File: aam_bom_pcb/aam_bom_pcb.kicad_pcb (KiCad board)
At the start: 4 copper layers, 58 x 19.5 mm, 42 parts, among them J1 USB_C_Receptacle_USB2.0_16P, U1 BQ25120AYFPR, U3 STM32WB5MMG, U4 TLV320DAC3203IRGER

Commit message: Actualización: integración de nuevos archivos al proyecto principal
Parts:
- moved TP6 23.1 mm to (179.9, 54.0)
- moved TP7 21.3 mm to (180.4, 50.5)
- moved C9 19.6 mm to (194.5, 52.5), turned to 180 degrees
- moved R8 19.4 mm to (187.2, 50.9), turned to 180 degrees
- moved C6 17.9 mm to (168.2, 49.9)
- moved C7 16.5 mm to (203.6, 63.1), turned to 180 degrees
- moved C17 15.3 mm to (182.5, 51.0), turned to -90 degrees
- moved C16 14.4 mm to (179.8, 59.0), turned to 180 degrees
- moved TP5 14.0 mm to (191.0, 48.0)
- moved C8 13.4 mm to (198.7, 52.5)
- moved L1 12.9 mm to (171.0, 47.9), turned to -90 degrees
- moved C18 12.1 mm to (182.1, 59.0), turned to 180 degrees
- moved C11 11.9 mm to (211.3, 53.1), turned to 180 degrees
- moved C5 10.7 mm to (172.0, 51.5)
- moved C10 10.7 mm to (198.7, 54.0), turned to 180 degrees
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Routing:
- net GND: track 0.00 -> 235.6 mm, vias 0 -> 40
- net +1V8: track 0.00 -> 123.1 mm, vias 0 -> 20
- net I2C_SDA: track 0.00 -> 44.7 mm, vias 0 -> 3
- net PDM_CLK: track 0.00 -> 41.1 mm, vias 0 -> 1
- net I2C_SCL: track 0.00 -> 39.6 mm, vias 0 -> 3
- net Net-(U3-VDDA): track 0.00 -> 28.1 mm, vias 0 -> 3
- net Net-(J1-SHIELD): track 0.00 -> 27.6 mm, vias 0 -> 4
- net /I2S_WCLK: track 0.00 -> 26.5 mm, vias 0 -> 2
- net Net-(D1-K): track 0.00 -> 19.4 mm, vias 0 -> 2
- net /I2S_DIN: track 0.00 -> 18.2 mm, vias 0 -> 2
- net /I2S_BCLK: track 0.00 -> 18.1 mm, vias 0 -> 2
- net PDM_DATA: track 0.00 -> 15.1 mm, vias 0 -> 2
- net Net-(U1-TS): track 0.00 -> 12.4 mm, vias 0 -> 2
- net Net-(U1-IN): track 0.00 -> 12.1 mm
- net VBAT: track 0.00 -> 7.83 mm, vias 0 -> 3
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
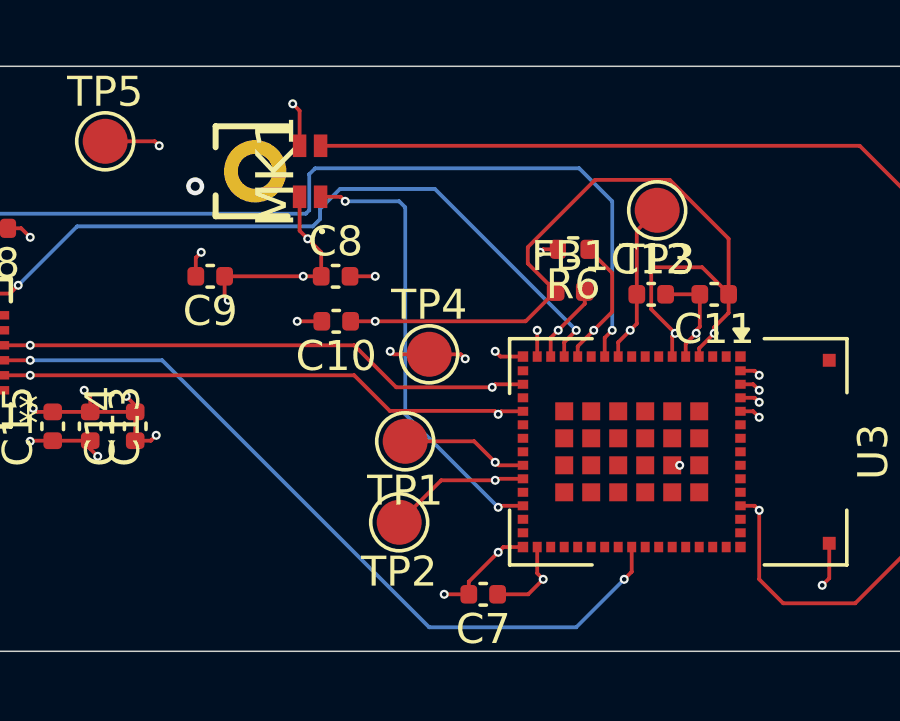
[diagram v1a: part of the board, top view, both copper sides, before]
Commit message: Integrar footprint de programación Tag-Connect TC2030-NL y validar esquemático
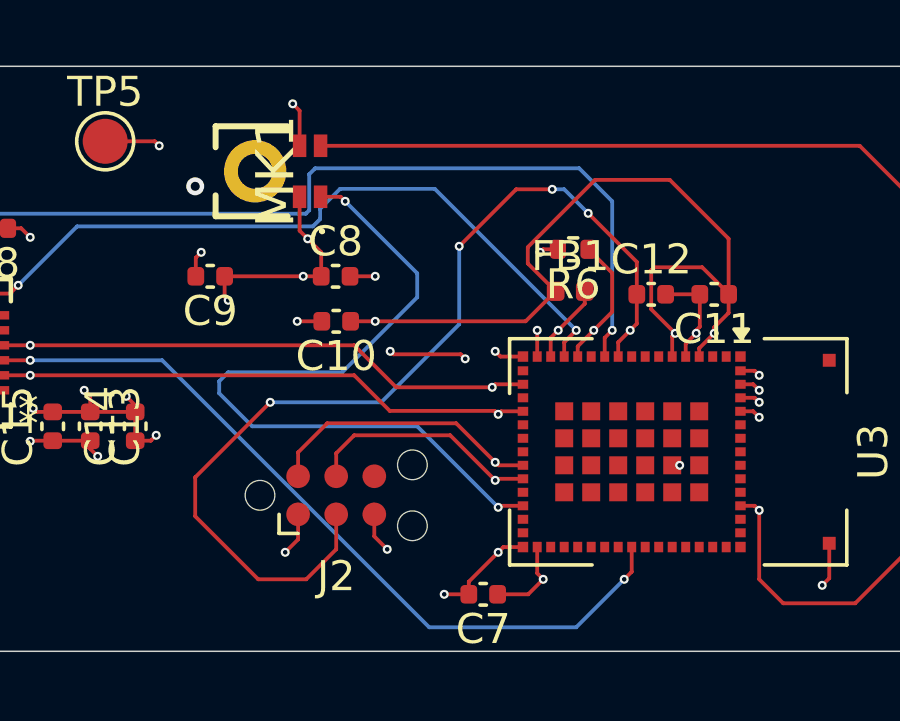
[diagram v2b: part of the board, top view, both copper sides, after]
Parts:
- removed TP1, TP2, TP3, TP4: TestPoint, TestPoint:TestPoint_Pad_D1.5mm
- added J2: Conn_ARM_SWD_TagConnect_TC2030-NL, Connector:Tag-Connect_TC2030-IDC-NL_2x03_P1.27mm_Vertical, F.Cu at (198.7, 59.8)
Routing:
- net /SWD_NRST: track 5.41 -> 33.1 mm, vias 1 -> 5
- net +1V8: track 123.1 -> 135.5 mm, vias 20 -> 21
- net PDM_DATA: track 15.1 -> 25.0 mm
- net /SWDIO: track 4.26 -> 9.27 mm
- net GND: track 235.6 -> 239.0 mm, vias 40 -> 41
- net /SWCLK: track 4.73 -> 7.88 mm
